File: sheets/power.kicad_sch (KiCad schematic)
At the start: 36 parts, among them J2 USB_C_Receptacle_USB2.0_16P, SW3 SW_SPDT, SW4 SW_SPST, U2 USBLC6-2P6, U3 TPS54620RGYR, U4 AMS1117-3.3, U5 LMR51430XFDDCR

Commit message: some footprints assigned
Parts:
- C28: footprint (none) -> Capacitor_SMD:C_0805_2012Metric
- FB2: footprint (none) -> Inductor_SMD:L_0805_2012Metric
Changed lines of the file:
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@@
 			)
 		)
-		(property "Footprint" ""
+		(property "Footprint" "Capacitor_SMD:C_0805_2012Metric"
 			(at 27.6352 172.72 0)
 			(effects
@@
 			)
 		)
-		(property "Footprint" ""
+		(property "Footprint" "Inductor_SMD:L_0805_2012Metric"
 			(at 74.422 36.83 90)
 			(effects

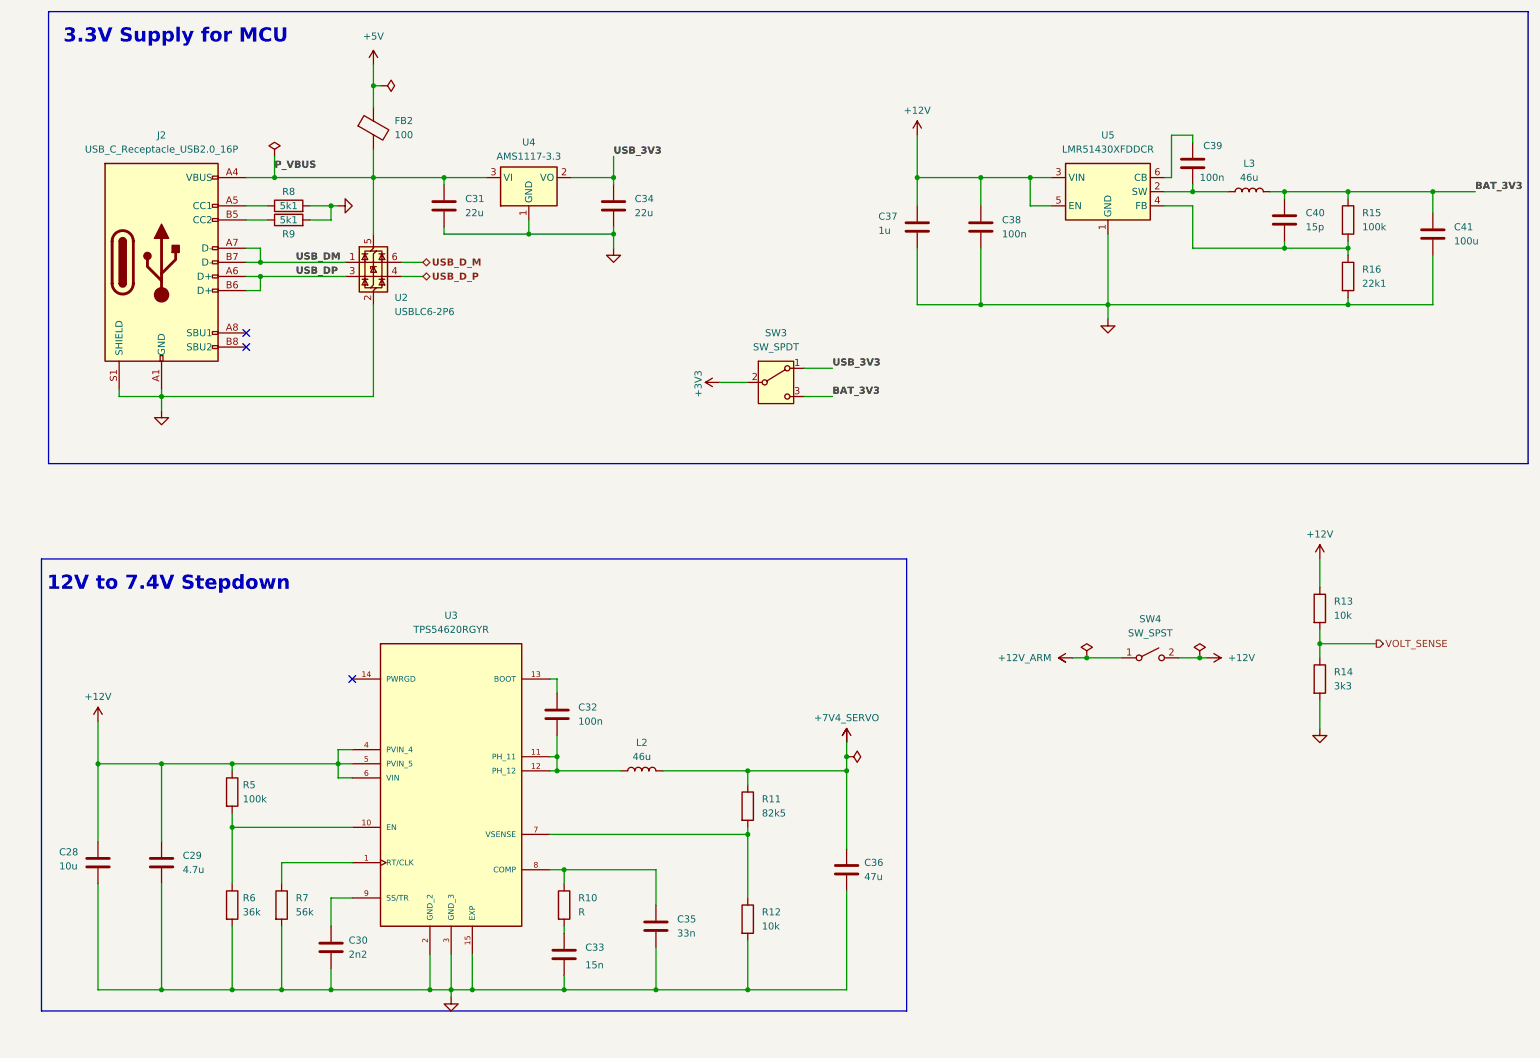
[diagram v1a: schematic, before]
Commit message: letter size schematic pages formatted
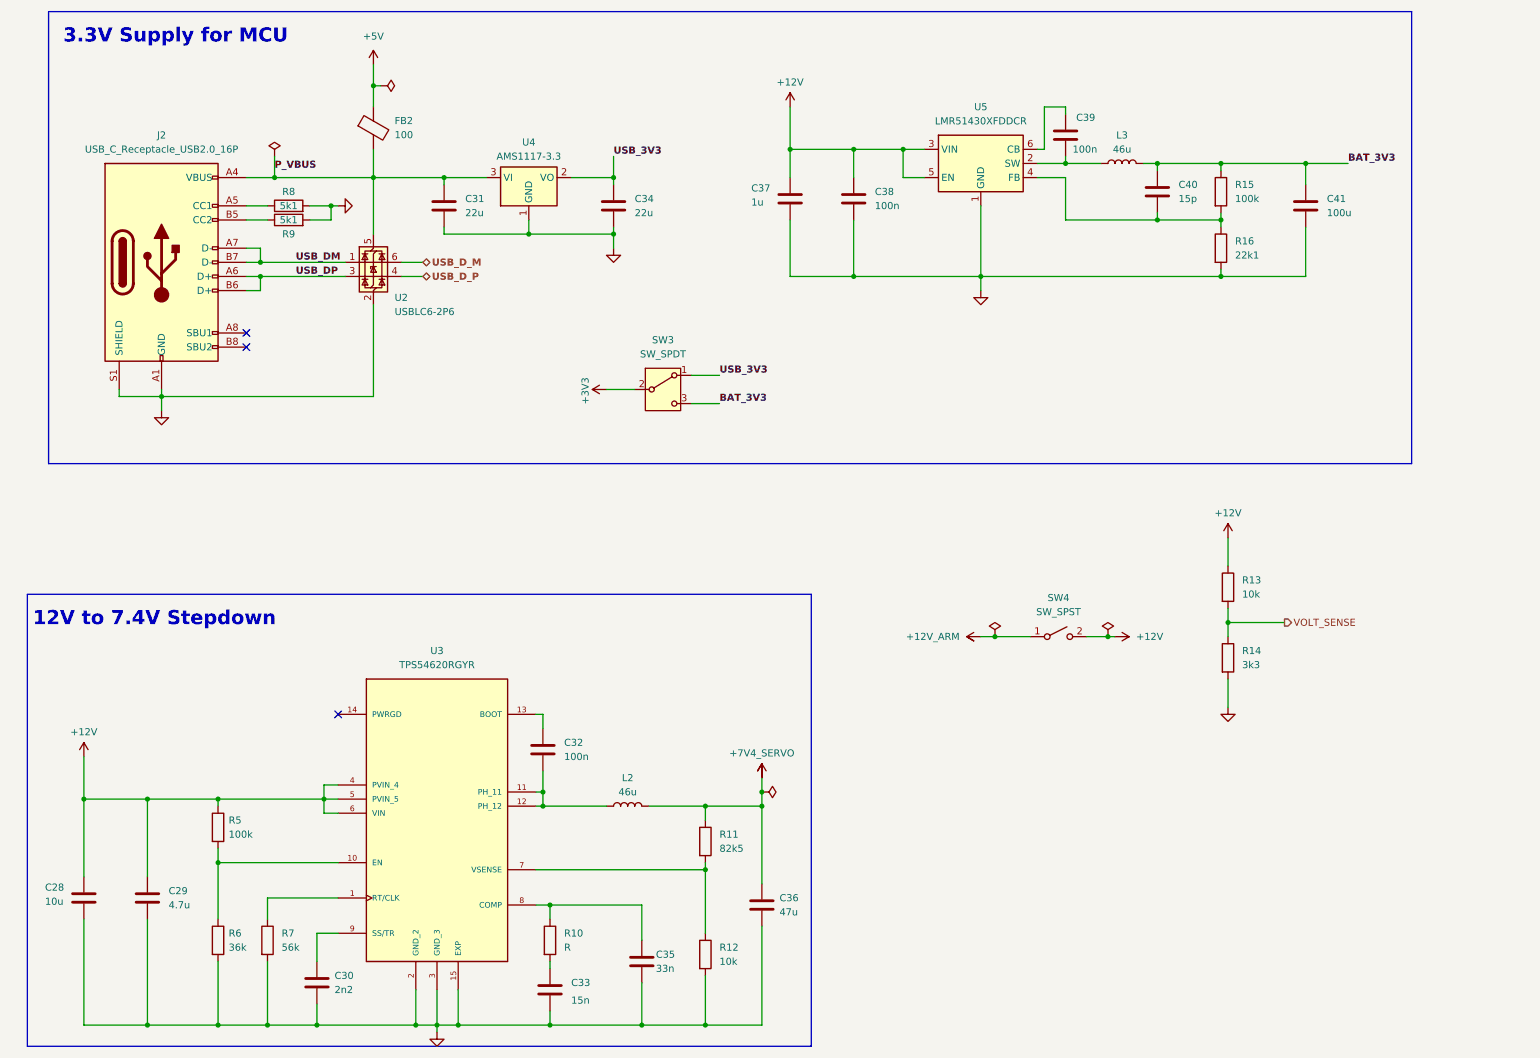
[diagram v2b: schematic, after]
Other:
- moved on the sheet: C28, C29, C30, C32, C33, C35, C36, C37, C38, C39, C40, C41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
